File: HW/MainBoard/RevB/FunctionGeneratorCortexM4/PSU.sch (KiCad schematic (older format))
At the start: 40 parts, among them Q1 DMG2301L, U1 NCP51460SN33T1G, U3 MCP1703A-3302_SOT223, U4 NCP1729, U5 NCP1729, U6 STM32G474RET

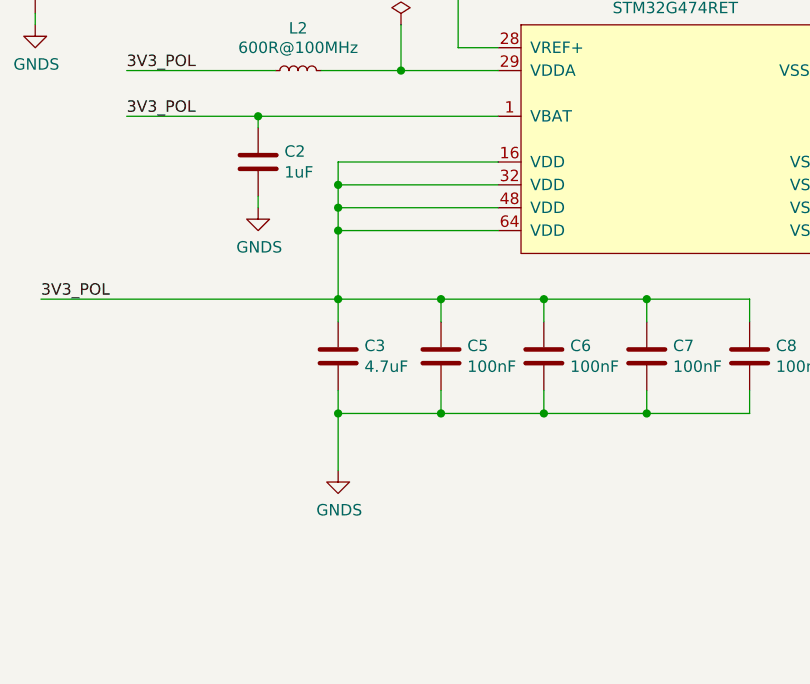
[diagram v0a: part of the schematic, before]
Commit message: REVB Update
- Changed TRIGIN J5 header to 2.54mm
- Changed IO J1 header to 2x05
- Added second charge pump IC
- Changed analog output circuit
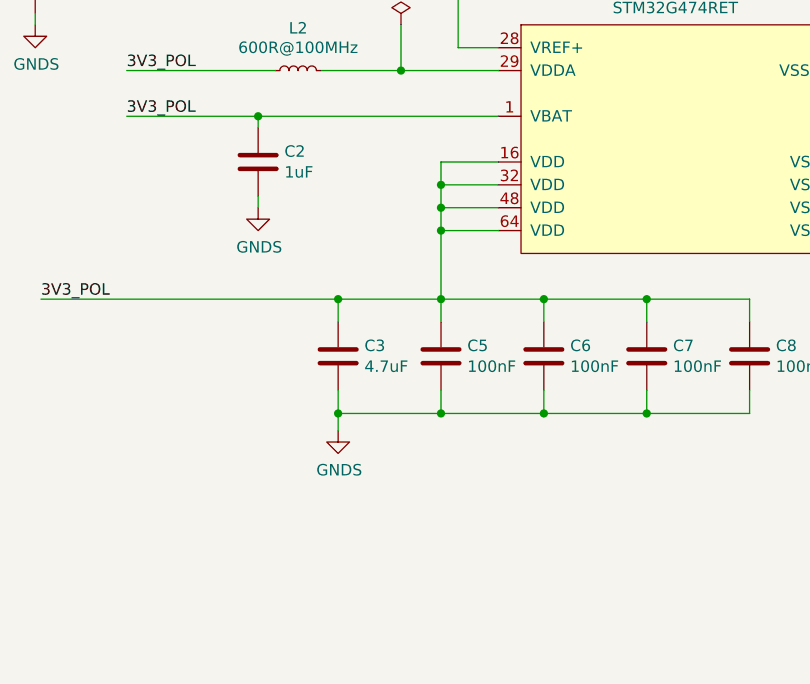
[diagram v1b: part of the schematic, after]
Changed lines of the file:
@@
 	7175 4650 7175 4600
 Wire Wire Line
-	8225 4800 7525 4800
-Wire Wire Line
-	7525 4800 7525 4900
+	8225 4800 7975 4800
+Wire Wire Line
+	7975 4800 7975 4900
 Wire Wire Line
 	9325 5400 8875 5400
 Wire Wire Line
-	8225 4900 7525 4900
-Connection ~ 7525 4900
-Wire Wire Line
-	7525 4900 7525 5000
-Wire Wire Line
-	7525 5000 8225 5000
-Connection ~ 7525 5000
-Wire Wire Line
-	7525 5000 7525 5100
-Wire Wire Line
-	8225 5100 7525 5100
+	8225 4900 7975 4900
+Connection ~ 7975 4900
+Wire Wire Line
+	7975 4900 7975 5000
+Wire Wire Line
+	7975 5000 8225 5000
+Connection ~ 7975 5000
+Wire Wire Line
+	7975 5000 7975 5100
+Wire Wire Line
+	8225 5100 7975 5100
 $Comp
 L Device:C C8
@@
 	7975 5900 8425 5900
 Wire Wire Line
-	7525 5900 7525 6150
+	7525 5900 7525 5975
 Connection ~ 7525 5900
 $Comp
 L power:GNDS #PWR0122
 U 1 1 5E655892
-P 7525 6150
-F 0 "#PWR0122" H 7525 5900 50  0001 C CNN
-F 1 "GNDS" H 7530 5977 50  0000 C CNN
-F 2 "" H 7525 6150 50  0001 C CNN
-F 3 "" H 7525 6150 50  0001 C CNN
-	1    7525 6150
+P 7525 5975
+F 0 "#PWR0122" H 7525 5725 50  0001 C CNN
+F 1 "GNDS" H 7530 5802 50  0000 C CNN
+F 2 "" H 7525 5975 50  0001 C CNN
+F 3 "" H 7525 5975 50  0001 C CNN
+	1    7525 5975
 	1    0    0    -1
 $EndComp
@@
 Wire Wire Line
 	6875 1400 7375 1400
-Wire Wire Line
-	7525 5100 7525 5400
-Connection ~ 7525 5100
 $Comp
 L power:GNDS #PWR0109
@@
 U 1 1 5F07B593
 P 3650 3600
-F 0 "#FLG?" H 3650 3675 50  0001 C CNN
+AR Path="/5EBB9B06/5F07B593" Ref="#FLG?"  Part="1"
+AR Path="/5E5FDE87/5F07B593" Ref="#FLG0102"  Part="1"
+F 0 "#FLG0102" H 3650 3675 50  0001 C CNN
 F 1 "PWR_FLAG" V 3650 3727 50  0000 L CNN
 F 2 "" H 3650 3600 50  0001 C CNN
@@
 	1    0    0    -1
 $EndComp
+Wire Wire Line
+	7975 5100 7975 5400
+Connection ~ 7975 5100
 $EndSCHEMATC

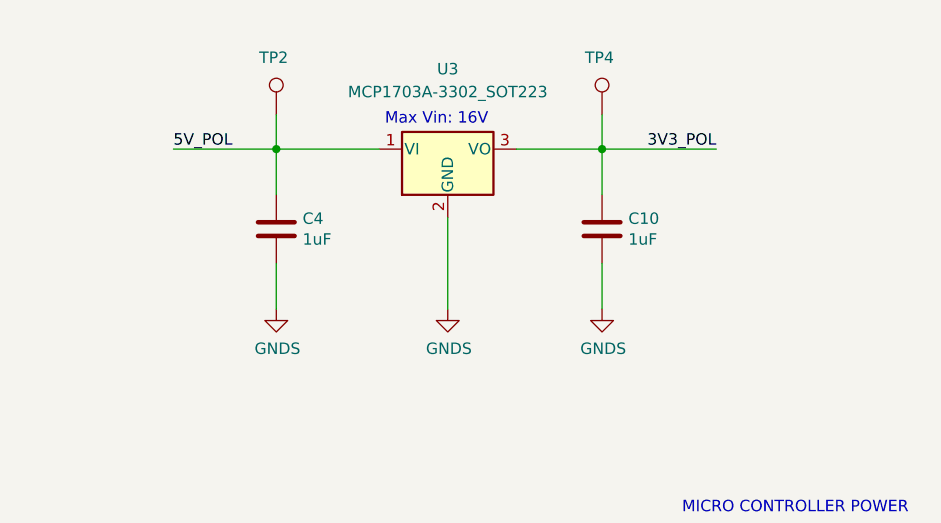
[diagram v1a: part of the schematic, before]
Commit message: Replaced LDO
changed SOT223 (MCP1703) to SO23-5 (LP3992)
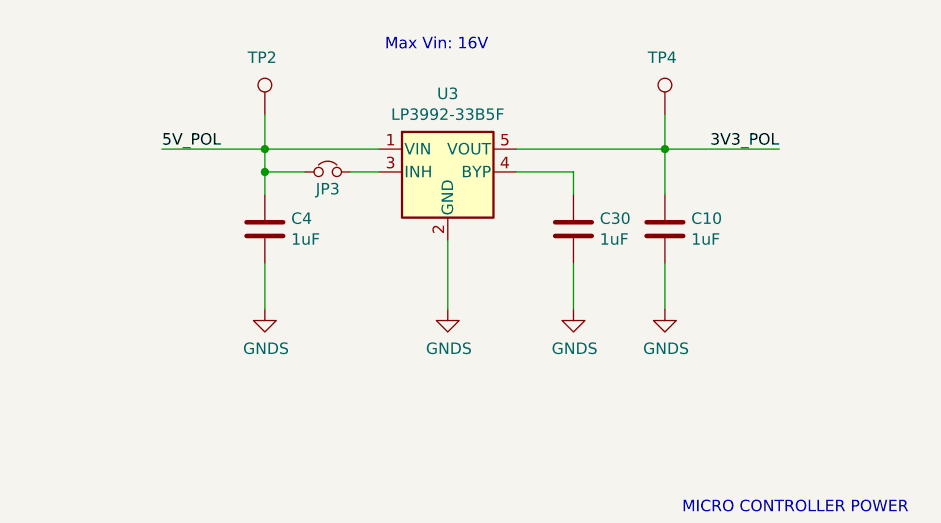
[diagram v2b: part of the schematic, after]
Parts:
- removed U3: MCP1703A-3302_SOT223, Package_TO_SOT_SMD:SOT-223-3_TabPin2, symbol Regulator_Linear:MCP1703A-3302_SOT223
- added C30: 1uF, Capacitor_SMD:C_1206_3216Metric_Pad1.42x1.75mm_HandSolder, symbol Device:C
- added JP3: Jumper_NC_Small, Jumper:SolderJumper-2_P1.3mm_Bridged_Pad1.0x1.5mm, symbol Device:Jumper_NC_Small
- added U3: LP3992-33B5F, Package_TO_SOT_SMD:TSOT-23-5, symbol Regulator_Linear:LD3985G33R_TSOT23
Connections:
- net +3V3: now also U3.5 (VOUT)
- net +5V: now also JP3.1, U3.1 (VIN)
- net GNDS: now also C30.2, U3.2 (GND)
- new net: JP3.2, U3.3 (INH)
- new net: C30.1, U3.4 (BYP)
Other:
- moved on the sheet: C10, C4, TP2, TP4
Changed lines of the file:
@@
 Wire Wire Line
 	9500 1125 9500 1300
-Text Label 5000 1400 0    50   ~ 0
+Text Label 4950 1400 0    50   ~ 0
 5V_POL
 $Comp
@@
 L Device:C C10
 U 1 1 5E61AAF1
-P 6875 1750
-F 0 "C10" H 6990 1796 50  0000 L CNN
-F 1 "1uF" H 6990 1705 50  0000 L CNN
-F 2 "Capacitor_SMD:C_1206_3216Metric_Pad1.42x1.75mm_HandSolder" H 6913 1600 50  0001 C CNN
-F 3 "~" H 6875 1750 50  0001 C CNN
-	1    6875 1750
-	1    0    0    -1
-$EndComp
-Wire Wire Line
-	6875 1600 6875 1400
-Wire Wire Line
-	6875 1900 6875 2100
+P 7150 1750
+F 0 "C10" H 7265 1796 50  0000 L CNN
+F 1 "1uF" H 7265 1705 50  0000 L CNN
+F 2 "Capacitor_SMD:C_1206_3216Metric_Pad1.42x1.75mm_HandSolder" H 7188 1600 50  0001 C CNN
+F 3 "~" H 7150 1750 50  0001 C CNN
+	1    7150 1750
+	1    0    0    -1
+$EndComp
+Wire Wire Line
+	7150 1600 7150 1400
+Wire Wire Line
+	7150 1900 7150 2100
 $Comp
 L power:GNDS #PWR0117
 U 1 1 5E61BDA3
-P 6875 2100
-F 0 "#PWR0117" H 6875 1850 50  0001 C CNN
-F 1 "GNDS" H 6880 1927 50  0000 C CNN
-F 2 "" H 6875 2100 50  0001 C CNN
-F 3 "" H 6875 2100 50  0001 C CNN
-	1    6875 2100
+P 7150 2100
+F 0 "#PWR0117" H 7150 1850 50  0001 C CNN
+F 1 "GNDS" H 7155 1927 50  0000 C CNN
+F 2 "" H 7150 2100 50  0001 C CNN
+F 3 "" H 7150 2100 50  0001 C CNN
+	1    7150 2100
 	1    0    0    -1
 $EndComp
@@
 L Device:C C4
 U 1 1 5E61EED5
-P 5450 1750
-F 0 "C4" H 5565 1796 50  0000 L CNN
-F 1 "1uF" H 5565 1705 50  0000 L CNN
-F 2 "Capacitor_SMD:C_1206_3216Metric_Pad1.42x1.75mm_HandSolder" H 5488 1600 50  0001 C CNN
-F 3 "~" H 5450 1750 50  0001 C CNN
-	1    5450 1750
-	1    0    0    -1
-$EndComp
-Wire Wire Line
-	5450 1900 5450 2100
+P 5400 1750
+F 0 "C4" H 5515 1796 50  0000 L CNN
+F 1 "1uF" H 5515 1705 50  0000 L CNN
+F 2 "Capacitor_SMD:C_1206_3216Metric_Pad1.42x1.75mm_HandSolder" H 5438 1600 50  0001 C CNN
+F 3 "~" H 5400 1750 50  0001 C CNN
+	1    5400 1750
+	1    0    0    -1
+$EndComp
+Wire Wire Line
+	5400 1900 5400 2100
 $Comp
 L power:GNDS #PWR0119
 U 1 1 5E61EEDC
-P 5450 2100
-F 0 "#PWR0119" H 5450 1850 50  0001 C CNN
-F 1 "GNDS" H 5455 1927 50  0000 C CNN
-F 2 "" H 5450 2100 50  0001 C CNN
-F 3 "" H 5450 2100 50  0001 C CNN
-	1    5450 2100
-	1    0    0    -1
-$EndComp
-Wire Wire Line
-	5450 1400 5450 1600
-Connection ~ 5450 1400
-Wire Wire Line
-	5450 1400 5000 1400
+P 5400 2100
+F 0 "#PWR0119" H 5400 1850 50  0001 C CNN
+F 1 "GNDS" H 5405 1927 50  0000 C CNN
+F 2 "" H 5400 2100 50  0001 C CNN
+F 3 "" H 5400 2100 50  0001 C CNN
+	1    5400 2100
+	1    0    0    -1
+$EndComp
+Wire Wire Line
+	5400 1400 5400 1500
+Connection ~ 5400 1400
+Wire Wire Line
+	5400 1400 4950 1400
 Wire Wire Line
 	4675 3750 5025 3750
@@
 Wire Wire Line
 	7250 4400 6600 4400
-Connection ~ 6875 1400
-Text Label 7375 1400 2    50   ~ 0
+Connection ~ 7150 1400
+Text Label 7650 1400 2    50   ~ 0
 3V3_POL
 $Comp
@@
 Text HLabel 10425 1100 1    50   Input ~ 0
 -5V
-Text Notes 5925 1300 0    50   ~ 0
-Max Vin: 16V
 Text Notes 5100 3600 0    50   ~ 0
 Max Vin: 28V
@@
 $EndComp
 Wire Wire Line
-	6200 1700 6200 2100
-Wire Wire Line
-	6875 1400 6500 1400
-Wire Wire Line
-	5450 1400 5900 1400
+	6200 1800 6200 2100
+Wire Wire Line
+	7150 1400 6500 1400
+Wire Wire Line
+	5400 1400 5900 1400
 $Comp
 L Transistor_FET:DMG2301L Q1
@@
 L Connector:TestPoint TP2
 U 1 1 5E5EDC2E
-P 5450 1250
-F 0 "TP2" H 5375 1500 50  0000 L CNN
-F 1 "TestPoint" H 5508 1277 50  0001 L CNN
-F 2 "TestPoint:TestPoint_Pad_1.0x1.0mm" H 5650 1250 50  0001 C CNN
-F 3 "~" H 5650 1250 50  0001 C CNN
-	1    5450 1250
-	1    0    0    -1
-$EndComp
-Wire Wire Line
-	5450 1250 5450 1400
+P 5400 1250
+F 0 "TP2" H 5325 1500 50  0000 L CNN
+F 1 "TestPoint" H 5458 1277 50  0001 L CNN
+F 2 "TestPoint:TestPoint_Pad_1.0x1.0mm" H 5600 1250 50  0001 C CNN
+F 3 "~" H 5600 1250 50  0001 C CNN
+	1    5400 1250
+	1    0    0    -1
+$EndComp
+Wire Wire Line
+	5400 1250 5400 1400
 $Comp
 L Connector:TestPoint TP4
 U 1 1 5E5F71A3
-P 6875 1250
-F 0 "TP4" H 6800 1500 50  0000 L CNN
-F 1 "TestPoint" H 6933 1277 50  0001 L CNN
-F 2 "TestPoint:TestPoint_Pad_1.0x1.0mm" H 7075 1250 50  0001 C CNN
-F 3 "~" H 7075 1250 50  0001 C CNN
-	1    6875 1250
-	1    0    0    -1
-$EndComp
-Wire Wire Line
-	6875 1250 6875 1400
+P 7150 1250
+F 0 "TP4" H 7075 1500 50  0000 L CNN
+F 1 "TestPoint" H 7208 1277 50  0001 L CNN
+F 2 "TestPoint:TestPoint_Pad_1.0x1.0mm" H 7350 1250 50  0001 C CNN
+F 3 "~" H 7350 1250 50  0001 C CNN
+	1    7150 1250
+	1    0    0    -1
+$EndComp
+Wire Wire Line
+	7150 1250 7150 1400
 $Comp
 L Connector:TestPoint TP3
@@
 Wire Wire Line
 	3225 3450 3225 3600
-$Comp
-L Regulator_Linear:MCP1703A-3302_SOT223 U3
-U 1 1 5E61840D
-P 6200 1400
-F 0 "U3" H 6200 1750 50  0000 C CNN
-F 1 "MCP1703A-3302_SOT223" H 6200 1650 50  0000 C CNN
-F 2 "Package_TO_SOT_SMD:SOT-223-3_TabPin2" H 6200 1600 50  0001 C CNN
-F 3 "http://ww1.microchip.com/downloads/en/DeviceDoc/20005122B.pdf" H 6200 1350 50  0001 C CNN
-	1    6200 1400
-	1    0    0    -1
-$EndComp
 $Comp
 L Device:LED D2
@@
 	2150 1225 2675 1225
 Wire Wire Line
-	6875 1400 7375 1400
+	7150 1400 7650 1400
 $Comp
 L power:GNDS #PWR0109
@@
 	7975 5100 7975 5400
 Connection ~ 7975 5100
+$Comp
+L Regulator_Linear:LD3985G33R_TSOT23 U3
+U 1 1 5E6E8CF6
+P 6200 1500
+F 0 "U3" H 6200 1842 50  0000 C CNN
+F 1 "LP3992-33B5F" H 6200 1751 50  0000 C CNN
+F 2 "Package_TO_SOT_SMD:TSOT-23-5" H 6200 1825 50  0001 C CIN
+F 3 "http://www.ti.com/lit/ds/symlink/lp3992.pdf" H 6200 1550 50  0001 C CNN
+	1    6200 1500
+	1    0    0    -1
+$EndComp
+Text Notes 5925 975  0    50   ~ 0
+Max Vin: 16V
+Wire Wire Line
+	5775 1500 5900 1500
+Wire Wire Line
+	5575 1500 5400 1500
+Connection ~ 5400 1500
+Wire Wire Line
+	5400 1500 5400 1600
+$Comp
+L Device:Jumper_NC_Small JP3
+U 1 1 5E721FFF
+P 5675 1500
+F 0 "JP3" H 5675 1425 50  0000 C CNN
+F 1 "Jumper_NC_Small" H 5675 1621 50  0001 C CNN
+F 2 "Jumper:SolderJumper-2_P1.3mm_Bridged_Pad1.0x1.5mm" H 5675 1500 50  0001 C CNN
+F 3 "~" H 5675 1500 50  0001 C CNN
+	1    5675 1500
+	1    0    0    -1
+$EndComp
+$Comp
+L Device:C C30
+U 1 1 5E73161C
+P 6750 1750
+F 0 "C30" H 6865 1796 50  0000 L CNN
+F 1 "1uF" H 6865 1705 50  0000 L CNN
+F 2 "Capacitor_SMD:C_1206_3216Metric_Pad1.42x1.75mm_HandSolder" H 6788 1600 50  0001 C CNN
+F 3 "~" H 6750 1750 50  0001 C CNN
+	1    6750 1750
+	1    0    0    -1
+$EndComp
+Wire Wire Line
+	6750 1900 6750 2100
+$Comp
+L power:GNDS #PWR011
+U 1 1 5E731624
+P 6750 2100
+F 0 "#PWR011" H 6750 1850 50  0001 C CNN
+F 1 "GNDS" H 6755 1927 50  0000 C CNN
+F 2 "" H 6750 2100 50  0001 C CNN
+F 3 "" H 6750 2100 50  0001 C CNN
+	1    6750 2100
+	1    0    0    -1
+$EndComp
+Wire Wire Line
+	6500 1500 6750 1500
+Wire Wire Line
+	6750 1500 6750 1600
 $EndSCHEMATC

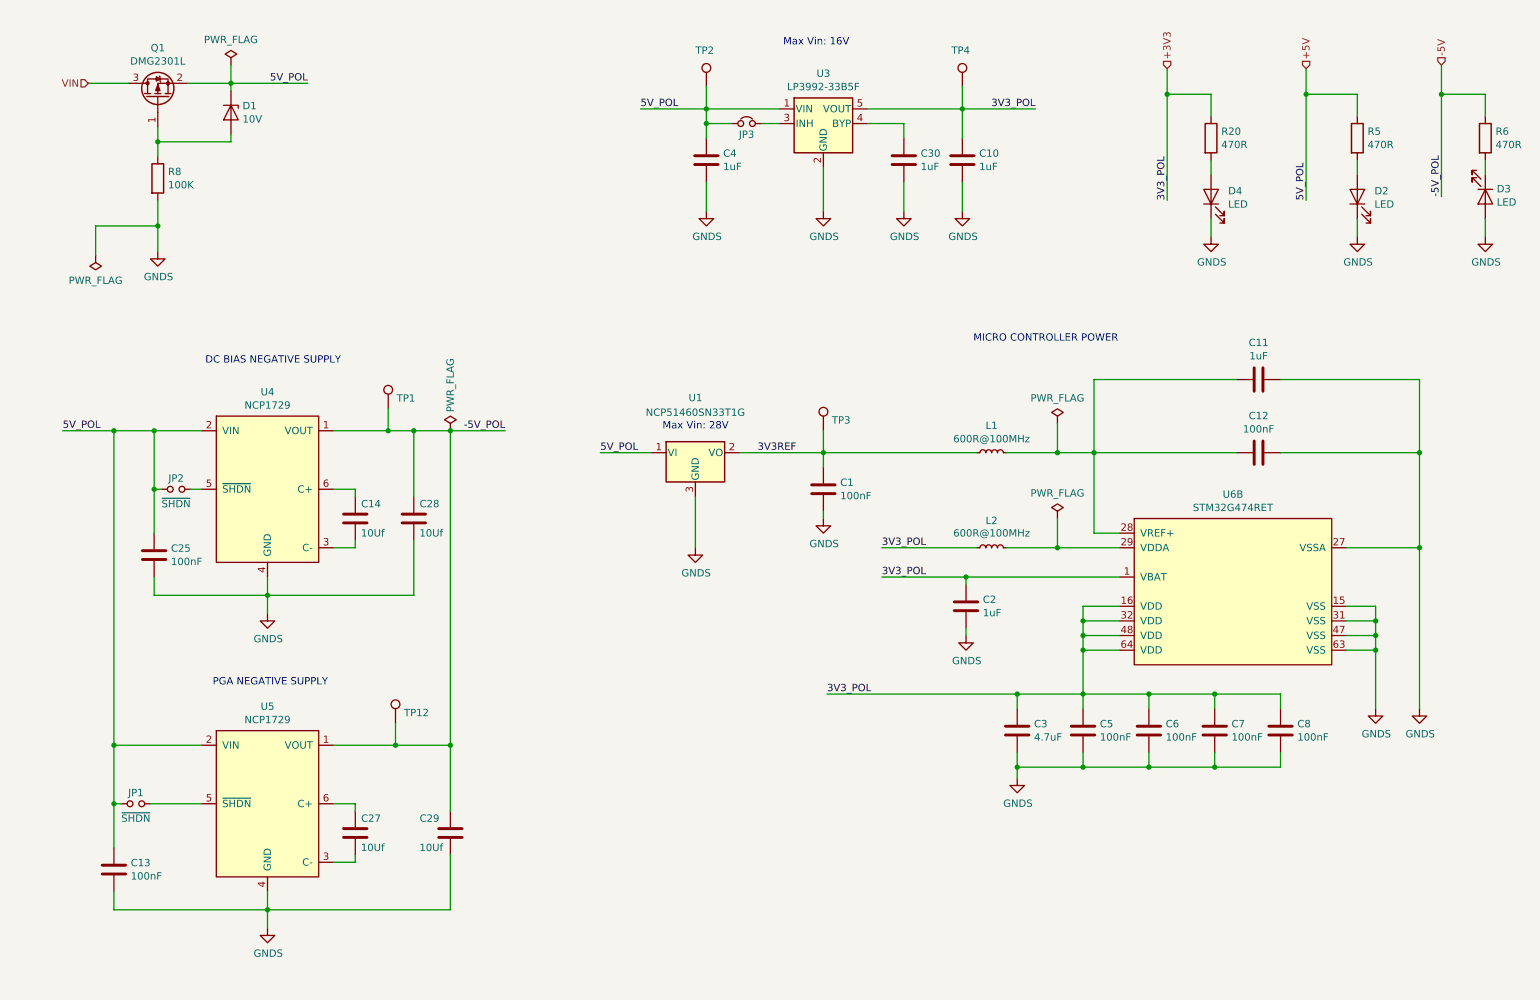
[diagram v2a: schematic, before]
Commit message: Modified PowerSupply section
- Added +2.5V ref
- Added Vin->5V LDO
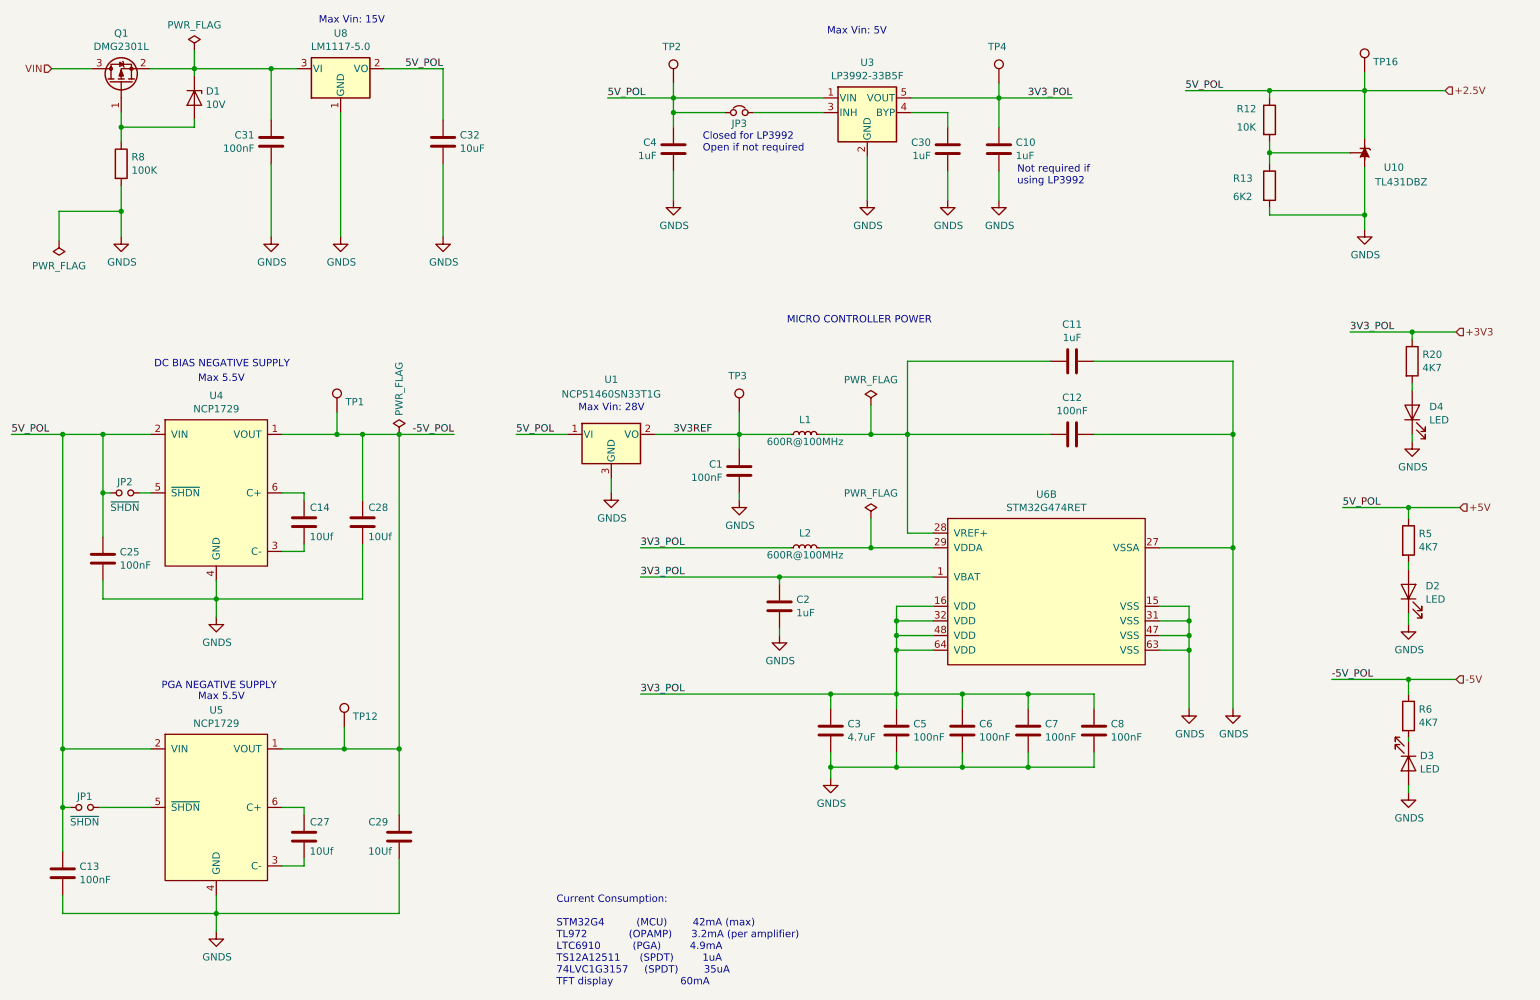
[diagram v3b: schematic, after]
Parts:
- added C31: 100nF, Capacitor_SMD:C_1206_3216Metric_Pad1.42x1.75mm_HandSolder, symbol Device:C
- added C32: 10uF, Capacitor_SMD:C_1206_3216Metric_Pad1.42x1.75mm_HandSolder, symbol Device:C
- added R12: 10K, Resistor_SMD:R_1206_3216Metric_Pad1.42x1.75mm_HandSolder, symbol Device:R
- added R13: 6K2, Resistor_SMD:R_1206_3216Metric_Pad1.42x1.75mm_HandSolder, symbol Device:R
- added TP16: TestPoint, TestPoint:TestPoint_Pad_1.0x1.0mm, symbol Connector:TestPoint
- added U10: TL431DBZ, Package_TO_SOT_SMD:SOT-23, symbol Reference_Voltage:TL431DBZ
- added U8: LM1117-5.0, symbol Regulator_Linear:LM1117-5.0
- C1, C11, C12, C14, C2, C27, C28, C29, C3, C5, C6, C7, C8: footprint Capacitor_SMD:C_0805_2012Metric_Pad1.15x1.40mm_HandSolder -> Capacitor_SMD:C_1206_3216Metric_Pad1.42x1.75mm_HandSolder
- R20, R5, R6: value 470R -> 4K7
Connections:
- net GNDS: now also C31.2, C32.2, R13.2, U10.3 (A), U8.1 (GND)
- net +5V renamed +2.5V
- net +2.5V: now also C32.1, R12.1, TP16.1, U10.1 (K), U8.2 (VO); no longer D1.1 (K), Q1.2 (S)
- new net: C31.1, D1.1 (K), Q1.2 (S), U8.3 (VI)
- new net: R12.2, R13.1, U10.2 (REF)
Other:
- note added: "Closed for LP3992\nOpen if not required"
- note added: "Current Consumption:\n\nSTM32G4 (MCU) 42mA (max)\nTL972 (OPAMP) 3.2mA (per amplifier)\nLTC6910 (PGA) 4.9mA\nTS12A12511 (SPDT) 1uA\n74LVC1G3157 (SPDT) 35uA\nTFT display 60mA"
- note added: "Max 5.5V"
- note added: "Max Vin: 15V"
- note added: "Max Vin: 5V"
- note added: "Not required if \nusing LP3992"
- note removed: "Max Vin: 16V"
- moved on the sheet: C1, C10, C11, C12, C13, C14, C2, C25, C27, C28, C29, C3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
